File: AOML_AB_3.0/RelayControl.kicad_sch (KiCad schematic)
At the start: 38 parts, among them IC1 CD4043BDR, IC2 CD4043BDR, J5 Conn_01x03, K1 TX2-L2-5V, K10 TX2-L2-5V, K11 TX2-L2-5V, K13 TX2-L2-5V, K2 TX2-L2-5V, K3 TX2-L2-5V, K4 TX2-L2-5V, K5 TX2-L2-5V, K6 TX2-L2-5V, K7 TX2-L2-5V, K8 TX2-L2-5V, K9 TX2-L2-5V, U10 TLP170AM, U11 TLP170AM, U12 TLP170AM, U13 TLP170AM, U14 TLP170AM, U15 TLP170AM, U16 TLP170AM, U17 TLP170AM, U5 ULN2003ADR

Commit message: PCB layout finished, next step is routing
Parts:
- removed RN3: 330, Resistor_network-330:RESCAV80P400X210X65-10N, symbol Device:R_Network08
- added RN4, RN5: R_Pack04, Resistor_network_x4_-330:RESCAXE80P320X160X70-8N, symbol Device:R_Pack04
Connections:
- net GND: now also RN4.1 (R1.1), RN4.2 (R2.1), RN4.3 (R3.1), RN4.4 (R4.1), RN5.1 (R1.1), RN5.2 (R2.1), RN5.3 (R3.1), RN5.4 (R4.1)
- net at U14.3: now also RN5.8 (R1.2)
- net at U12.3: now also RN4.6 (R3.2)
- net at U13.3: now also RN4.5 (R4.2)
- net at U15.3: now also RN5.7 (R2.2)
- net at U17.3: now also RN5.5 (R4.2)
- net at U16.3: now also RN5.6 (R3.2)
- net at U11.3: now also RN4.7 (R2.2)
- net at U10.3: now also RN4.8 (R1.2)
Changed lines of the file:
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@@
   (junction (at 331.47 110.49) (diameter 0) (color 0 0 0 0)
   )
+  (junction (at 341.63 236.22) (diameter 0) (color 0 0 0 0)
+  )
   (junction (at 138.43 110.49) (diameter 0) (color 0 0 0 0)
   )
@@
   (junction (at 396.24 189.23) (diameter 0) (color 0 0 0 0)
   )
+  (junction (at 344.17 236.22) (diameter 0) (color 0 0 0 0)
+  )
   (junction (at 138.43 137.16) (diameter 0) (color 0 0 0 0)
   )
@@
   (junction (at 220.98 196.85) (diameter 0) (color 0 0 0 0)
   )
+  (junction (at 355.6 236.22) (diameter 0) (color 0 0 0 0)
+  )
   (junction (at 143.51 223.52) (diameter 0) (color 0 0 0 0)
   )
@@
   (junction (at 143.51 153.67) (diameter 0) (color 0 0 0 0)
   )
+  (junction (at 353.06 236.22) (diameter 0) (color 0 0 0 0)
+  )
   (junction (at 193.04 142.24) (diameter 0) (color 0 0 0 0)
   )
@@
   (junction (at 396.24 167.64) (diameter 0) (color 0 0 0 0)
   )
+  (junction (at 346.71 236.22) (diameter 0) (color 0 0 0 0)
+  )
   (junction (at 198.12 153.67) (diameter 0) (color 0 0 0 0)
   )
   (junction (at 151.13 241.3) (diameter 0) (color 0 0 0 0)
   )
+  (junction (at 349.25 236.22) (diameter 0) (color 0 0 0 0)
+  )
+  (junction (at 350.52 236.22) (diameter 0) (color 0 0 0 0)
+  )
   (junction (at 151.13 228.6) (diameter 0) (color 0 0 0 0)
   )
@@
     (stroke (width 0) (type default))
   )
-  (wire (pts (xy 345.44 226.06) (xy 345.44 107.95))
+  (wire (pts (xy 344.17 226.06) (xy 344.17 107.95))
     (stroke (width 0) (type default))
   )
@@
     (stroke (width 0) (type default))
   )
-  (wire (pts (xy 340.36 226.06) (xy 340.36 64.77))
+  (wire (pts (xy 339.09 226.06) (xy 339.09 64.77))
     (stroke (width 0) (type default))
   )
@@
     (stroke (width 0) (type default))
   )
+  (wire (pts (xy 344.17 236.22) (xy 346.71 236.22))
+    (stroke (width 0) (type default))
+  )
   (wire (pts (xy 77.47 173.99) (xy 157.48 173.99))
     (stroke (width 0) (type default))
@@
     (stroke (width 0) (type default))
   )
-  (wire (pts (xy 345.44 107.95) (xy 358.14 107.95))
+  (wire (pts (xy 344.17 107.95) (xy 358.14 107.95))
     (stroke (width 0) (type default))
   )
@@
     (stroke (width 0) (type default))
   )
-  (wire (pts (xy 347.98 226.06) (xy 347.98 129.54))
+  (wire (pts (xy 346.71 226.06) (xy 346.71 129.54))
     (stroke (width 0) (type default))
   )
@@
     (stroke (width 0) (type default))
   )
-  (wire (pts (xy 340.36 64.77) (xy 358.14 64.77))
+  (wire (pts (xy 339.09 64.77) (xy 358.14 64.77))
     (stroke (width 0) (type default))
   )
@@
     (stroke (width 0) (type default))
   )
+  (wire (pts (xy 341.63 236.22) (xy 344.17 236.22))
+    (stroke (width 0) (type default))
+  )
   (wire (pts (xy 133.35 194.31) (xy 144.78 194.31))
     (stroke (width 0) (type default))
@@
     (stroke (width 0) (type default))
   )
-  (wire (pts (xy 342.9 226.06) (xy 342.9 86.36))
+  (wire (pts (xy 341.63 226.06) (xy 341.63 86.36))
     (stroke (width 0) (type default))
   )
@@
     (stroke (width 0) (type default))
   )
+  (wire (pts (xy 355.6 236.22) (xy 358.14 236.22))
+    (stroke (width 0) (type default))
+  )
   (wire (pts (xy 135.89 189.23) (xy 135.89 184.15))
     (stroke (width 0) (type default))
@@
     (stroke (width 0) (type default))
   )
-  (wire (pts (xy 347.98 129.54) (xy 358.14 129.54))
+  (wire (pts (xy 346.71 129.54) (xy 358.14 129.54))
     (stroke (width 0) (type default))
   )
@@
     (stroke (width 0) (type default))
   )
+  (wire (pts (xy 353.06 236.22) (xy 355.6 236.22))
+    (stroke (width 0) (type default))
+  )
   (wire (pts (xy 198.12 153.67) (xy 203.2 153.67))
     (stroke (width 0) (type default))
@@
     (stroke (width 0) (type default))
   )
-  (wire (pts (xy 342.9 86.36) (xy 358.14 86.36))
+  (wire (pts (xy 341.63 86.36) (xy 358.14 86.36))
     (stroke (width 0) (type default))
   )
@@
     (stroke (width 0) (type default))
   )
+  (wire (pts (xy 339.09 236.22) (xy 341.63 236.22))
+    (stroke (width 0) (type default))
+  )
   (wire (pts (xy 396.24 189.23) (xy 396.24 210.82))
     (stroke (width 0) (type default))
@@
     (stroke (width 0) (type default))
   )
+  (wire (pts (xy 346.71 236.22) (xy 349.25 236.22))
+    (stroke (width 0) (type default))
+  )
   (wire (pts (xy 396.24 102.87) (xy 373.38 102.87))
     (stroke (width 0) (type default))
@@
     (stroke (width 0) (type default))
   )
+  (wire (pts (xy 350.52 236.22) (xy 353.06 236.22))
+    (stroke (width 0) (type default))
+  )
   (wire (pts (xy 325.12 186.69) (xy 331.47 186.69))
     (stroke (width 0) (type default))
@@
     (stroke (width 0) (type default))
   )
+  (wire (pts (xy 349.25 236.22) (xy 349.25 238.76))
+    (stroke (width 0) (type default))
+  )
   (wire (pts (xy 187.96 173.99) (xy 198.12 173.99))
     (stroke (width 0) (type default))
@@
     (stroke (width 0) (type default))
   )
+  (wire (pts (xy 349.25 236.22) (xy 350.52 236.22))
+    (stroke (width 0) (type default))
+  )
   (wire (pts (xy 290.83 97.79) (xy 294.64 97.79))
     (stroke (width 0) (type default))
@@
     )
   )
-  (symbol (lib_id "power:GND") (at 358.14 236.22 0) (unit 1)
+  (symbol (lib_id "power:GND") (at 349.25 238.76 0) (unit 1)
     (in_bom yes) (on_board yes) (dnp no) (fields_autoplaced)
-    (property "Reference" "#PWR087" (at 358.14 242.57 0)
+    (property "Reference" "#PWR087" (at 349.25 245.11 0)
       (effects (font (size 1.27 1.27)) hide)
     )
-    (property "Value" "GND" (at 358.14 241.3 0)
+    (property "Value" "GND" (at 349.25 243.84 0)
       (effects (font (size 1.27 1.27)))
     )
-    (property "Footprint" "" (at 358.14 236.22 0)
+    (property "Footprint" "" (at 349.25 238.76 0)
       (effects (font (size 1.27 1.27)) hide)
     )
-    (property "Datasheet" "" (at 358.14 236.22 0)
+    (property "Datasheet" "" (at 349.25 238.76 0)
       (effects (font (size 1.27 1.27)) hide)
     )
@@
     )
   )
+  (symbol (lib_id "Device:R_Pack04") (at 355.6 231.14 0) (unit 1)
+    (in_bom yes) (on_board yes) (dnp no) (fields_autoplaced)
+    (property "Reference" "RN5" (at 360.68 229.87 0)
+      (effects (font (size 1.27 1.27)) (justify left))
+    )
+    (property "Value" "R_Pack04" (at 360.68 232.41 0)
+      (effects (font (size 1.27 1.27)) (justify left))
+    )
+    (property "Footprint" "Resistor_network_x4_-330:RESCAXE80P320X160X70-8N" (at 362.585 231.14 90)
+      (effects (font (size 1.27 1.27)) hide)
+    )
+    (property "Datasheet" "https://www.yageo.com/upload/media/product/app/datasheet/rchip/pyu-yc_tc_group_51_rohs_l.pdf" (at 355.6 231.14 0)
+      (effects (font (size 1.27 1.27)) hide)
+    )
+    (property "Digikey" "https://www.digikey.com/en/products/detail/yageo/YC164-JR-07330RL/1005112" (at 355.6 231.14 0)
+      (effects (font (size 1.27 1.27)) hide)
+    )
+    (pin "1")
+    (pin "2")
+    (pin "3")
+    (pin "4")
+    (pin "5")
+    (pin "6")
+    (pin "7")
+    (pin "8")
+    (instances
+      (project "AOML_AB_3.0"
+        (path "/6a222f58-627e-41ff-951d-9ad8d2e0d7a2/69365a30-fc6f-418a-bc31-d76af2fc83f6"
+          (reference "RN5") (unit 1)
+        )
+      )
+    )
+  )
   (symbol (lib_id "Connector_Generic:Conn_01x03") (at 248.92 148.59 180) (unit 1)
     (in_bom yes) (on_board yes) (dnp no) (fields_autoplaced)
@@
     )
   )
-  (symbol (lib_id "Device:R_Network08") (at 347.98 231.14 180) (unit 1)
-    (in_bom yes) (on_board yes) (dnp no) (fields_autoplaced)
-    (property "Reference" "RN3" (at 360.68 229.616 0)
-      (effects (font (size 1.27 1.27)) (justify right))
-    )
-    (property "Value" "330" (at 360.68 232.156 0)
-      (effects (font (size 1.27 1.27)) (justify right))
-    )
-    (property "Footprint" "Resistor_network-330:RESCAV80P400X210X65-10N" (at 335.915 231.14 90)
-      (effects (font (size 1.27 1.27)) hide)
-    )
-    (property "Datasheet" "https://industrial.panasonic.com/ww/products/pt/resistor-network-array/models/EXBE10C331J" (at 347.98 231.14 0)
-      (effects (font (size 1.27 1.27)) hide)
-    )
-    (property "Digikey" "https://www.digikey.com/en/products/detail/panasonic-electronic-components/EXB-E10C331J/282888" (at 347.98 231.14 0)
-      (effects (font (size 1.27 1.27)) hide)
-    )
-    (pin "1")
-    (pin "2")
-    (pin "3")
-    (pin "4")
-    (pin "5")
-    (pin "6")
-    (pin "7")
-    (pin "8")
-    (pin "9")
-    (instances
-      (project "AOML_AB_3.0"
-        (path "/6a222f58-627e-41ff-951d-9ad8d2e0d7a2"
-          (reference "RN3") (unit 1)
-        )
-        (path "/6a222f58-627e-41ff-951d-9ad8d2e0d7a2/69365a30-fc6f-418a-bc31-d76af2fc83f6"
-          (reference "RN4") (unit 1)
-        )
-      )
-    )
-  )
   (symbol (lib_id "Relay_SolidState:TLP175A") (at 365.76 62.23 0) (unit 1)
     (in_bom yes) (on_board yes) (dnp no) (fields_autoplaced)
@@
         )
       )
+    )
+  )
+  (symbol (lib_id "Device:R_Pack04") (at 344.17 231.14 0) (unit 1)
+    (in_bom yes) (on_board yes) (dnp no) (fields_autoplaced)
+    (property "Reference" "RN4" (at 349.25 229.87 0)
+      (effects (font (size 1.27 1.27)) (justify left))
+    )
+    (property "Value" "R_Pack04" (at 349.25 232.41 0)
+      (effects (font (size 1.27 1.27)) (justify left))
+    )
+    (property "Footprint" "Resistor_network_x4_-330:RESCAXE80P320X160X70-8N" (at 351.155 231.14 90)
+      (effects (font (size 1.27 1.27)) hide)
+    )
+    (property "Datasheet" "https://www.yageo.com/upload/media/product/app/datasheet/rchip/pyu-yc_tc_group_51_rohs_l.pdf" (at 344.17 231.14 0)
+      (effects (font (size 1.27 1.27)) hide)
+    )
+    (property "Digikey" "https://www.digikey.com/en/products/detail/yageo/YC164-JR-07330RL/1005112" (at 344.17 231.14 0)
+      (effects (font (size 1.27 1.27)) hide)
+    )
+    (pin "1")
+    (pin "2")
+    (pin "3")
+    (pin "4")
+    (pin "5")
+    (pin "6")
+    (pin "7")
+    (pin "8")
+    (instances
+      (project "AOML_AB_3.0"
+        (path "/6a222f58-627e-41ff-951d-9ad8d2e0d7a2/69365a30-fc6f-418a-bc31-d76af2fc83f6"
+          (reference "RN4") (unit 1)
+        )
+      )

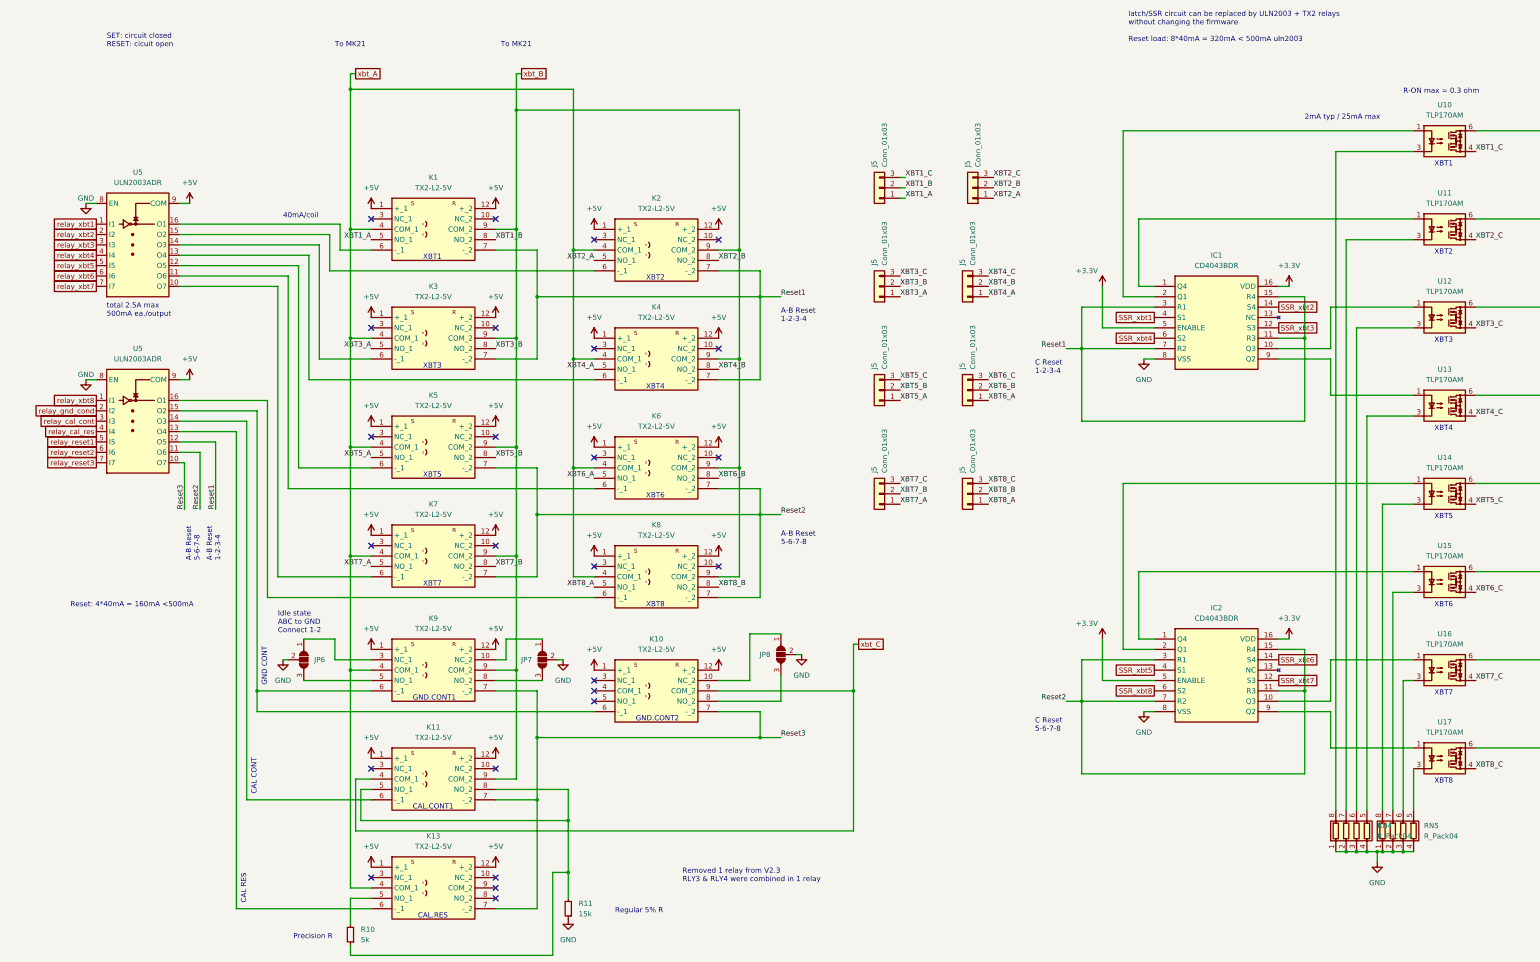
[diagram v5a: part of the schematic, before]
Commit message: PCB reorganized for better routing, R networks changed to x4, power leds added, micro outputs need relocation to allow easier routing to each side
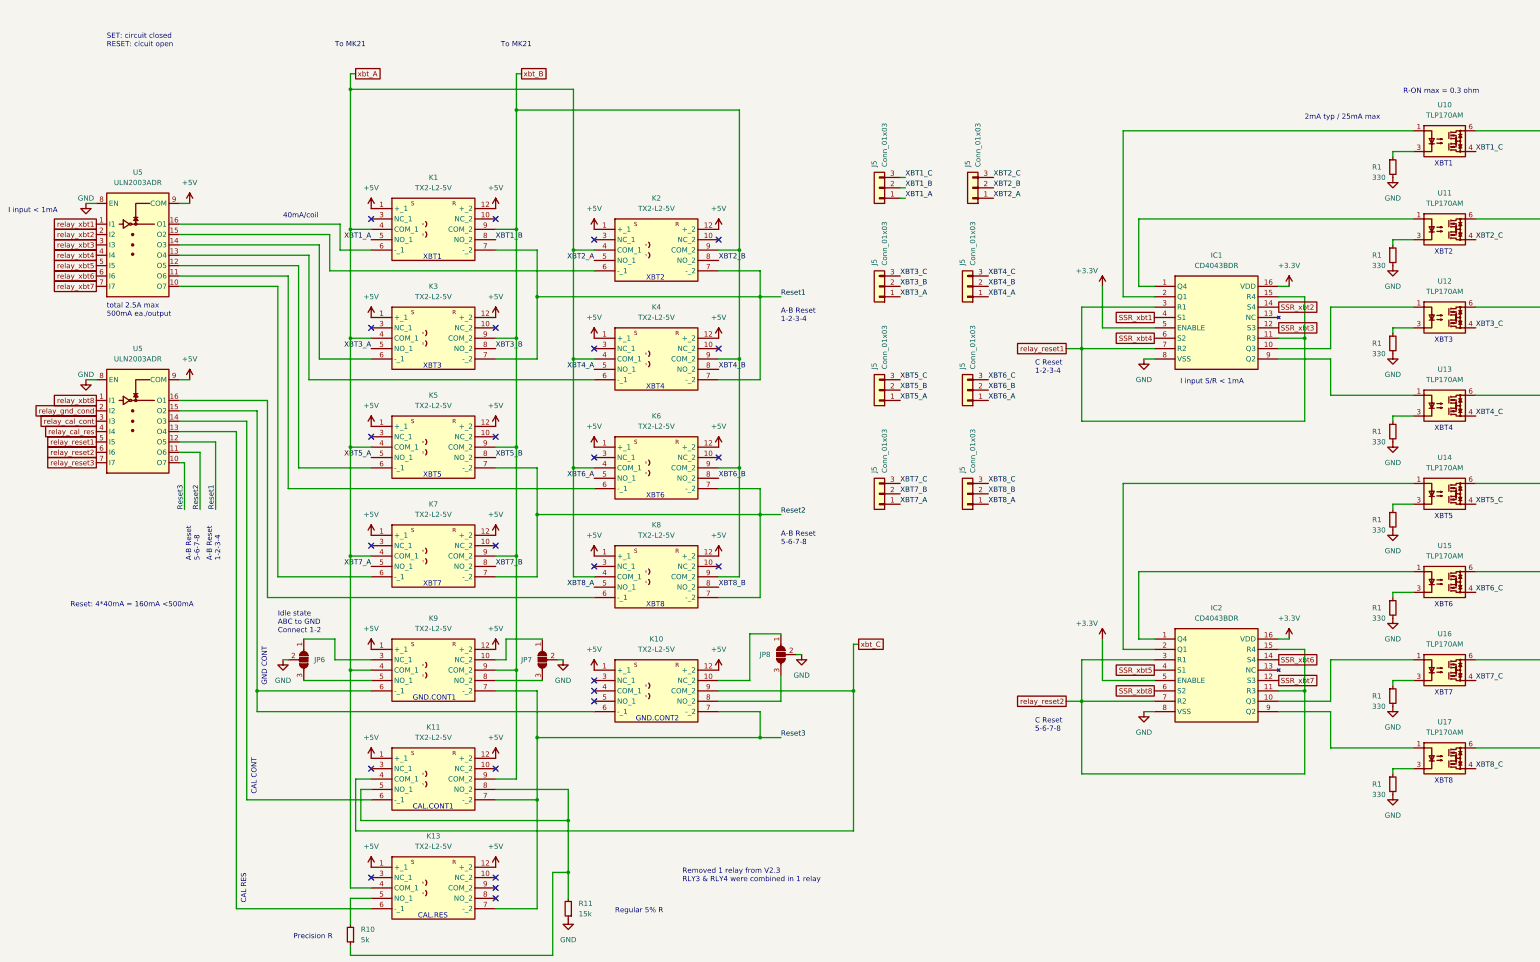
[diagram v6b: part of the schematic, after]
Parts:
- removed RN4, RN5: R_Pack04, Resistor_network_x4_-330:RESCAXE80P320X160X70-8N, symbol Device:R_Pack04
- added R1 (x8): 330, Resistor_0805:RC0805N_YAG, symbol Device:R_Small
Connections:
- net GND: now also R1.2, R1.2, R1.2, R1.2, R1.2, R1.2, R1.2, R1.2
- net Reset1: no longer IC1.11 (R3), IC1.15 (R4), IC1.3 (R1), IC1.7 (R2)
- net Reset2: no longer IC2.11 (R3), IC2.15 (R4), IC2.3 (R1), IC2.7 (R2)
- net relay_reset1: now also IC1.11 (R3), IC1.15 (R4), IC1.3 (R1), IC1.7 (R2)
- net relay_reset2: now also IC2.11 (R3), IC2.15 (R4), IC2.3 (R1), IC2.7 (R2)
- net at U14.3: now also R1.1
- net at U12.3: now also R1.1
- net at U13.3: now also R1.1
- net at U17.3: now also R1.1
- net at U16.3: now also R1.1
- net at U15.3: now also R1.1
- net at U10.3: now also R1.1
- net at U11.3: now also R1.1
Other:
- note added: "I input < 1mA"
- note added: "I input S/R < 1mA"
- note removed: "latch/SSR circuit can be replaced by ULN2003 + TX2 relays without changing the firmware Reset load: 8*40mA = 320mA < 500mA uln2003"
